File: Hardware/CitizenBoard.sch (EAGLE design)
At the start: 30 parts, among them IC1 MEGA8-P, J1 DCJ0202, J2 AUDIO-JACK-3.5, Y1 16MHz

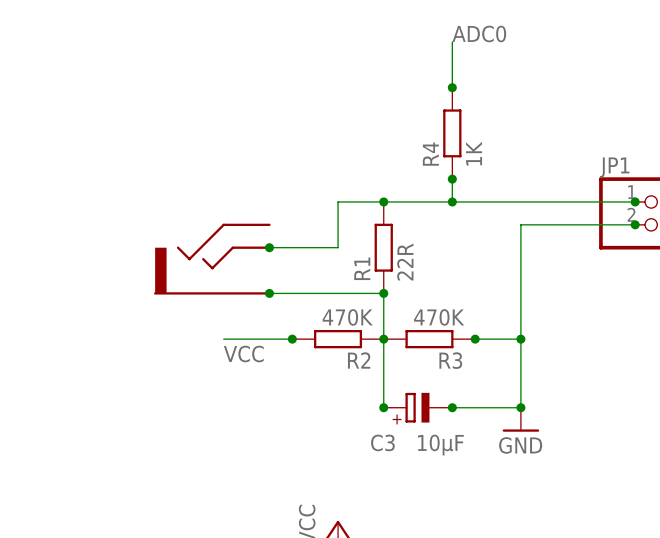
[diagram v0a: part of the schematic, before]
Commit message: Correction de l'empreinte du jack
Et modification de tracés pour le champ de masse
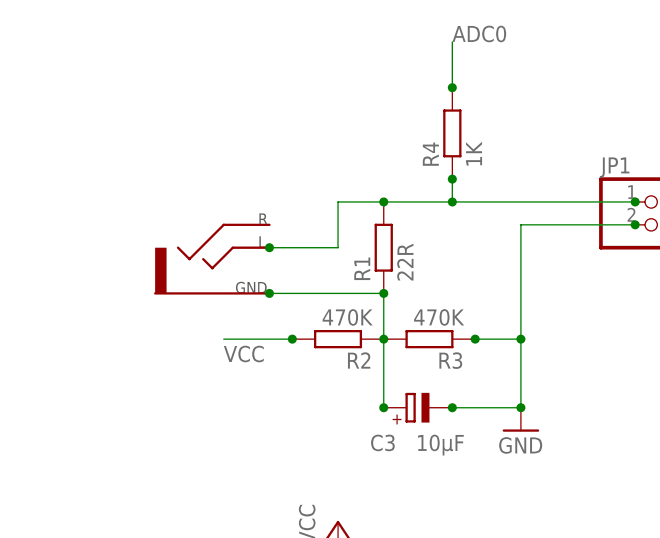
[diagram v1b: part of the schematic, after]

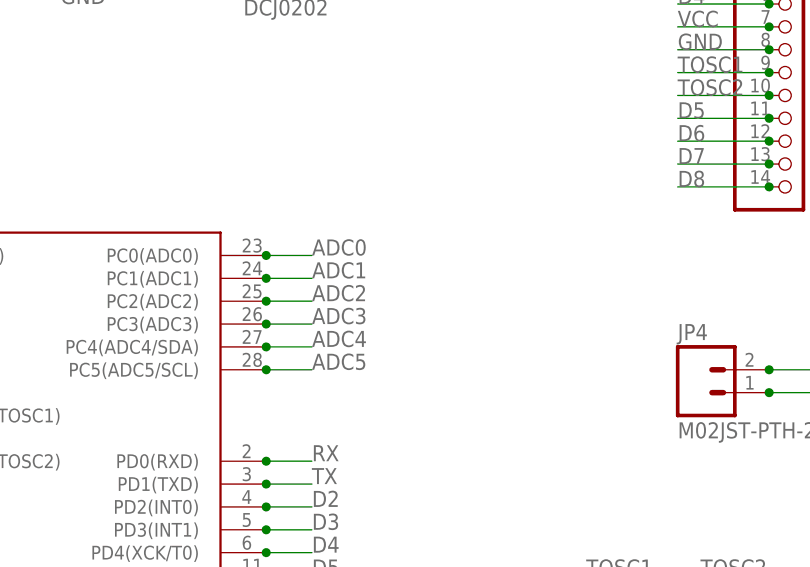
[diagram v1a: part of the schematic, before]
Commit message: Mesure de la valeur de la batterie
via un solder pad
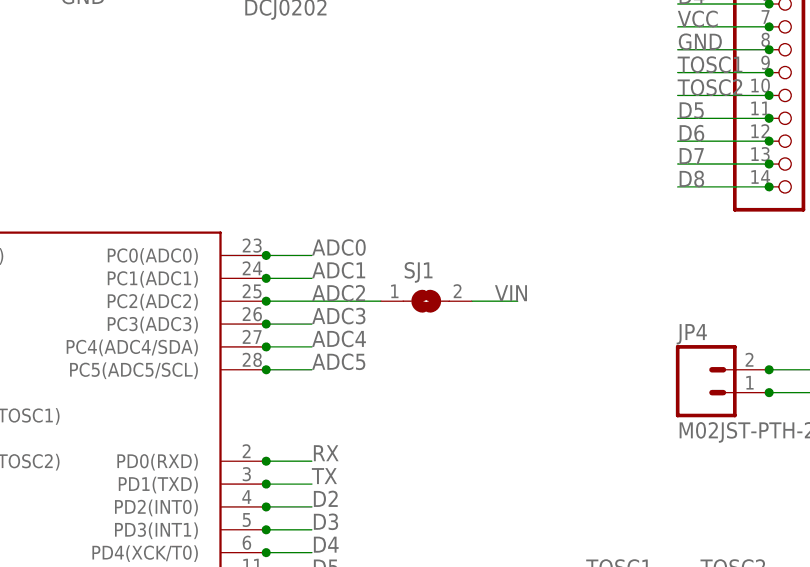
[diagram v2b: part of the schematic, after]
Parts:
- added SJ1: (no value), jumper:SJ
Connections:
- net ADC2: now also SJ1.1
- net VIN: now also SJ1.2
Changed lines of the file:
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@@
 <part name="C5" library="rcl" deviceset="CPOL-EU" device="E2,5-6E" value="10uF"/>
 <part name="JP5" library="pinhead" deviceset="PINHD-1X4" device=""/>
+<part name="SJ1" library="jumper" deviceset="SJ" device=""/>
 </parts>
 <sheets>
@@
 <instance part="C5" gate="G$1" x="198.12" y="45.72"/>
 <instance part="JP5" gate="A" x="172.72" y="43.18"/>
+<instance part="SJ1" gate="1" x="116.84" y="53.34"/>
 </instances>
 <busses>
@@
 <segment>
 <pinref part="IC1" gate="G$1" pin="PC2(ADC2)"/>
-<wire x1="99.06" y1="53.34" x2="104.14" y2="53.34" width="0.1524" layer="91"/>
 <junction x="99.06" y="53.34"/>
 <label x="104.14" y="53.34" size="1.778" layer="95"/>
+<pinref part="SJ1" gate="1" pin="1"/>
+<wire x1="99.06" y1="53.34" x2="111.76" y2="53.34" width="0.1524" layer="91"/>
 </segment>
 <segment>
@@
 <junction x="170.18" y="45.72"/>
 </segment>
-</net>
+<segment>
+<pinref part="SJ1" gate="1" pin="2"/>
+<wire x1="121.92" y1="53.34" x2="127" y2="53.34" width="0.1524" layer="91"/>
+<label x="124.46" y="53.34" size="1.778" layer="95"/>
+</segment>
+</net>
